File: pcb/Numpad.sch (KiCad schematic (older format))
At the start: 61 parts, among them P1 USB-MICRO-B, P2 HOLE, P3 HOLE, P4 HOLE, P5 HOLE, SW1 F13, SW10 8, SW11 9, SW12 PLUS, SW13 4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

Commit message: Macrofab order
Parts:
- C2, C3: value 18p -> 8p
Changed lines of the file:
@@
 P 5650 5150
 F 0 "C2" H 5675 5250 50  0000 L CNN
-F 1 "18p" H 5675 5050 50  0000 L CNN
+F 1 "8p" H 5675 5050 50  0000 L CNN
 F 2 "Keyboard:C_0805" H 5688 5000 50  0001 C CNN
 F 3 "" H 5650 5150 50  0000 C CNN
@@
 P 6550 5150
 F 0 "C3" H 6575 5250 50  0000 L CNN
-F 1 "18p" H 6575 5050 50  0000 L CNN
+F 1 "8p" H 6575 5050 50  0000 L CNN
 F 2 "Keyboard:C_0805" H 6588 5000 50  0001 C CNN
 F 3 "" H 6550 5150 50  0000 C CNN
@@
 $EndComp
 $Comp
-L +5V #PWR09
+L +5V #PWR08
 U 1 1 57D75692
 P 10000 5000
-F 0 "#PWR09" H 10000 4850 50  0001 C CNN
+F 0 "#PWR08" H 10000 4850 50  0001 C CNN
 F 1 "+5V" H 10000 5140 50  0000 C CNN
 F 2 "" H 10000 5000 50  0000 C CNN
@@
 $EndComp
 $Comp
-L GND #PWR010
+L GND #PWR09
 U 1 1 57D75718
 P 10000 5600
-F 0 "#PWR010" H 10000 5350 50  0001 C CNN
+F 0 "#PWR09" H 10000 5350 50  0001 C CNN
 F 1 "GND" H 10000 5450 50  0000 C CNN
 F 2 "" H 10000 5600 50  0000 C CNN
@@
 $EndComp
 $Comp
-L GND #PWR012
+L GND #PWR010
 U 1 1 583FE5A3
 P 8150 4850
-F 0 "#PWR012" H 8150 4600 50  0001 C CNN
+F 0 "#PWR010" H 8150 4600 50  0001 C CNN
 F 1 "GND" H 8150 4700 50  0000 C CNN
 F 2 "" H 8150 4850 50  0000 C CNN
@@
 $EndComp
 $Comp
-L GND #PWR013
+L GND #PWR011
 U 1 1 583F8B57
 P 6100 4950
-F 0 "#PWR013" H 6100 4700 50  0001 C CNN
+F 0 "#PWR011" H 6100 4700 50  0001 C CNN
 F 1 "GND" H 6100 4800 50  0000 C CNN
 F 2 "" H 6100 4950 50  0000 C CNN
@@
 $EndComp
 $Comp
-L GND #PWR014
+L GND #PWR012
 U 1 1 5840D946
 P 9450 3900
-F 0 "#PWR014" H 9450 3650 50  0001 C CNN
+F 0 "#PWR012" H 9450 3650 50  0001 C CNN
 F 1 "GND" H 9450 3750 50  0000 C CNN
 F 2 "" H 9450 3900 50  0000 C CNN
@@
 $EndComp
 $Comp
-L +5V #PWR015
+L +5V #PWR013
 U 1 1 587461EE
 P 5700 1000
-F 0 "#PWR015" H 5700 850 50  0001 C CNN
+F 0 "#PWR013" H 5700 850 50  0001 C CNN
 F 1 "+5V" H 5700 1140 50  0000 C CNN
 F 2 "" H 5700 1000 50  0000 C CNN
@@
 $EndComp
 $Comp
-L +5V #PWR016
+L +5V #PWR014
 U 1 1 5874632C
 P 6050 2700
-F 0 "#PWR016" H 6050 2550 50  0001 C CNN
+F 0 "#PWR014" H 6050 2550 50  0001 C CNN
 F 1 "+5V" H 6050 2840 50  0000 C CNN
 F 2 "" H 6050 2700 50  0000 C CNN

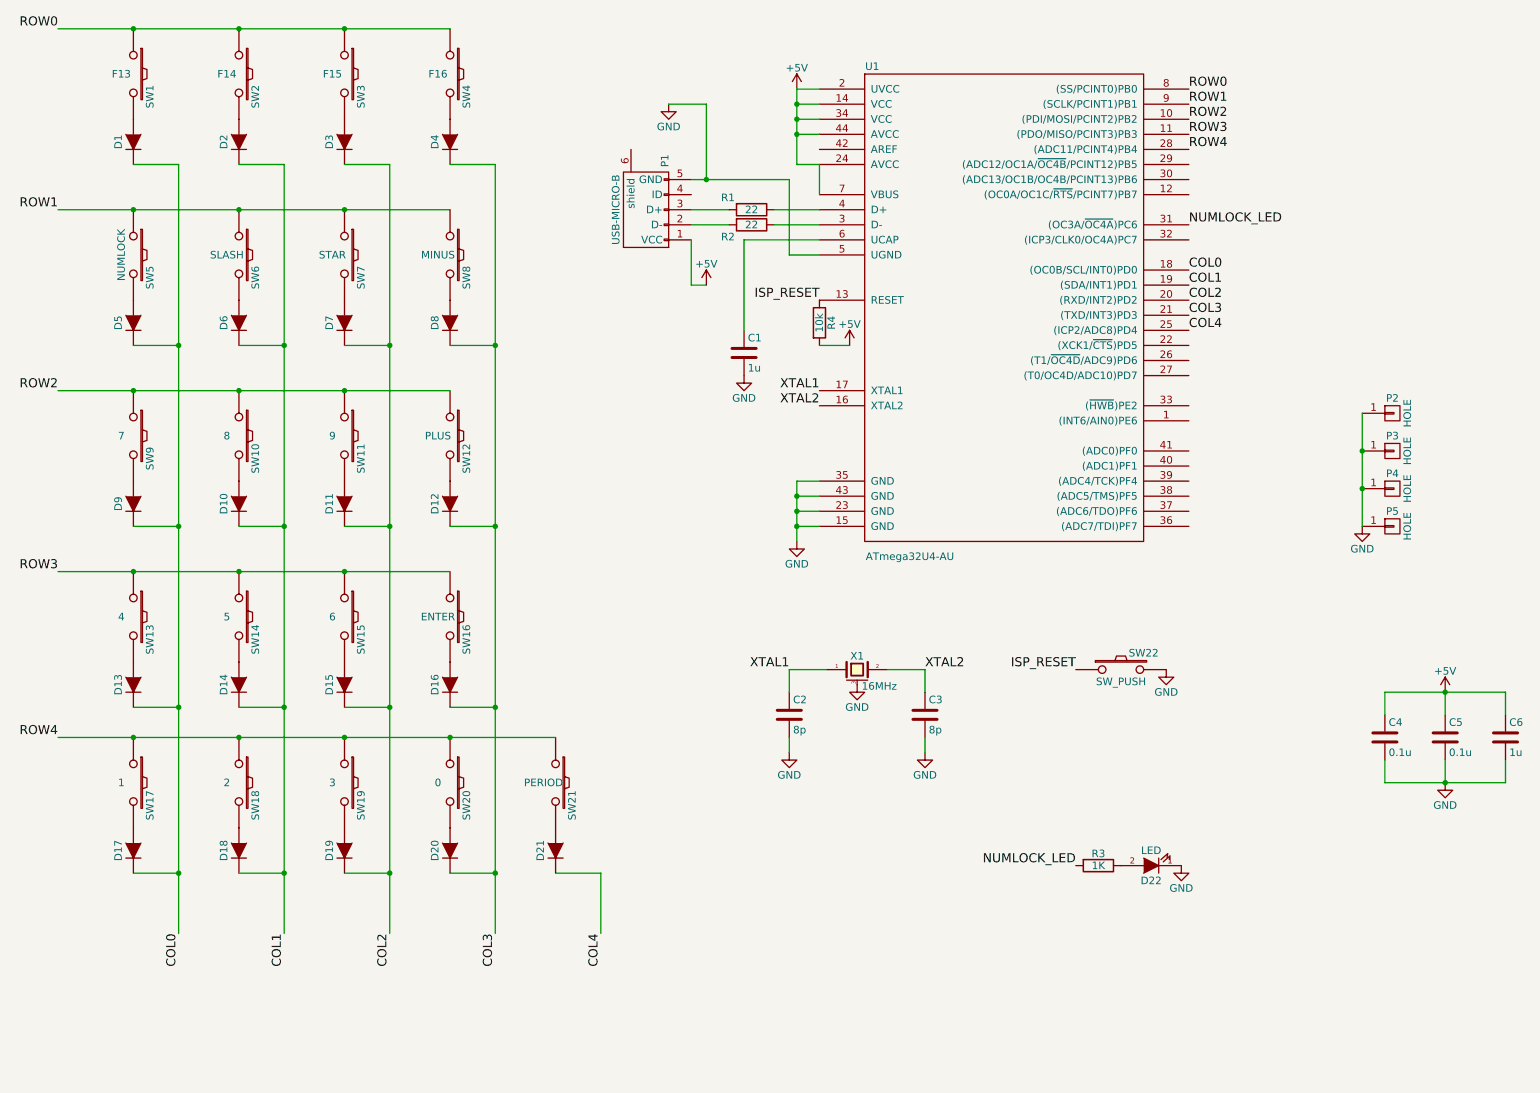
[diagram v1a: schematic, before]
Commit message: Remove atmega32u4 and related components
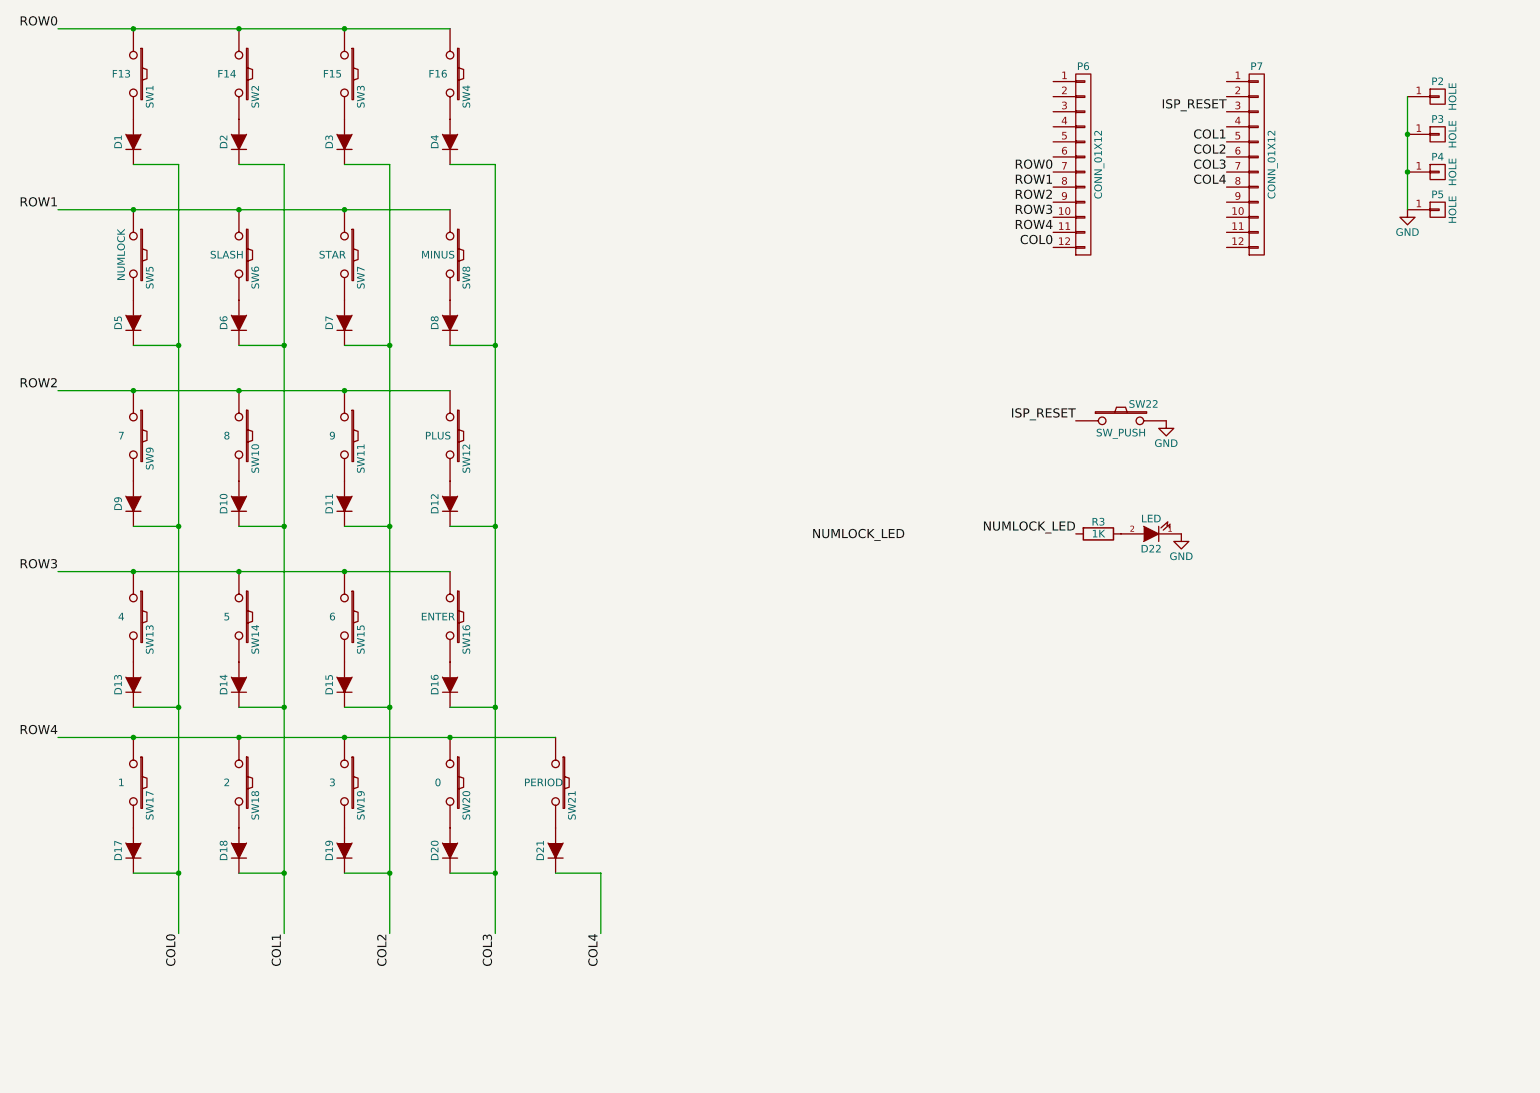
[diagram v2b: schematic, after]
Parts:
- removed C1, C6: 1u, Keyboard:C_0805, symbol C
- removed C2, C3: 8p, Keyboard:C_0805, symbol C
- removed C4, C5: 0.1u, Keyboard:C_0805, symbol C
- removed P1: USB-MICRO-B, 10118192-0001LF:10118192-0001LF, symbol USB_OTG
- removed R1, R2: 22, Keyboard:R_0805, symbol R
- removed R4: 10k, Keyboard:R_0805, symbol R
- removed U1: ATmega32U4-AU, ATMEGA32U4-AU:QFP80P1200X1200X120-44N, symbol ATmega32U4-AU
- removed X1: 16MHz, Crystals:Crystal_SMD_5032_4Pads, symbol CRYSTAL_SMD
- added P6, P7: CONN_01X12, Pin_Headers:Pin_Header_Straight_1x12_Pitch2.54mm, symbol CONN_01X12
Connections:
- net COL0: now also P6.12 (P12)
- net COL1: now also P7.5 (P5)
- net COL2: now also P7.6 (P6)
- net COL3: now also P7.7 (P7)
- net COL4: now also P7.8 (P8)
- net ISP_RESET: now also P7.3 (P3)
- net ROW0: now also P6.7 (P7)
- net ROW1: now also P6.8 (P8)
- net ROW2: now also P6.9 (P9)
- net ROW3: now also P6.10 (P10)
- net ROW4: now also P6.11 (P11)
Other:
- moved on the sheet: D22, P2, P3, P4, P5, R3, SW22

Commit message: Complete routes and layout. Need to check Osh Park rules
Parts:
- removed D3, D4: D, Diodes_SMD:SOD-123, symbol D
- removed SW3: F15, Tim's Cherry MX:CHERRY_PLATE_100H, symbol SW_PUSH
- removed SW4: F16, Tim's Cherry MX:CHERRY_PLATE_100H, symbol SW_PUSH
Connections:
- net COL0: now also P6.11 (P11); no longer P6.12 (P12)
- net COL1: now also P6.10 (P10); no longer P7.5 (P5)
- net COL2: now also P6.8 (P8); no longer P7.6 (P6)
- net COL3: now also P7.6 (P6); no longer P7.7 (P7)
- net COL4: now also P7.5 (P5); no longer P7.8 (P8)
- net GND: now also P7.2 (P2)
- net ROW0: now also P6.12 (P12); no longer P6.7 (P7)
- net ROW1: now also P6.9 (P9); no longer P6.8 (P8)
- net ROW2: now also P6.7 (P7); no longer P6.9 (P9)
- net ROW3: now also P7.8 (P8); no longer P6.10 (P10)
- net ROW4: now also P7.7 (P7); no longer P6.11 (P11)
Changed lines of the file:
@@
-$EndComp
-$Comp
-L SW_PUSH SW3
-U 1 1 57D60E45
-P 2700 900
-F 0 "SW3" H 2850 1010 50  0000 C CNN
-F 1 "F15" V 2700 820 50  0000 C CNN
-F 2 "Tim's Cherry MX:CHERRY_PLATE_100H" H 2700 900 50  0001 C CNN
-F 3 "" H 2700 900 50  0000 C CNN
-	1    2700 900
-	0    1    1    0
-$EndComp
-$Comp
-L SW_PUSH SW4
-U 1 1 57D60E4B
-P 3400 900
-F 0 "SW4" H 3550 1010 50  0000 C CNN
-F 1 "F16" V 3400 820 50  0000 C CNN
-F 2 "Tim's Cherry MX:CHERRY_PLATE_100H" H 3400 900 50  0001 C CNN
-F 3 "" H 3400 900 50  0000 C CNN
-	1    3400 900
-	0    1    1    0
 $EndComp
 $Comp
@@
 F 3 "" H 2000 1350 50  0000 C CNN
 	1    2000 1350
-	0    -1   -1   0
-$EndComp
-$Comp
-L D D3
-U 1 1 57D61BB8
-P 2700 1350
-F 0 "D3" H 2700 1450 50  0000 C CNN
-F 1 "D" H 2700 1250 50  0001 C CNN
-F 2 "Diodes_SMD:SOD-123" H 2700 1350 50  0001 C CNN
-F 3 "" H 2700 1350 50  0000 C CNN
-	1    2700 1350
-	0    -1   -1   0
-$EndComp
-$Comp
-L D D4
-U 1 1 57D61C02
-P 3400 1350
-F 0 "D4" H 3400 1450 50  0000 C CNN
-F 1 "D" H 3400 1250 50  0001 C CNN
-F 2 "Diodes_SMD:SOD-123" H 3400 1350 50  0001 C CNN
-F 3 "" H 3400 1350 50  0000 C CNN
-	1    3400 1350
 	0    -1   -1   0
 $EndComp
@@
 $EndComp
 $Comp
-L GND #PWR04
+L GND #PWR02
 U 1 1 583FE5A3
 P 8150 3200
-F 0 "#PWR04" H 8150 2950 50  0001 C CNN
+F 0 "#PWR02" H 8150 2950 50  0001 C CNN
 F 1 "GND" H 8150 3050 50  0000 C CNN
 F 2 "" H 8150 3200 50  0000 C CNN
@@
 $EndComp
 $Comp
-L GND #PWR05
+L GND #PWR03
 U 1 1 5840D946
 P 9750 1800
-F 0 "#PWR05" H 9750 1550 50  0001 C CNN
+F 0 "#PWR03" H 9750 1550 50  0001 C CNN
 F 1 "GND" H 9750 1650 50  0000 C CNN
 F 2 "" H 9750 1800 50  0000 C CNN
@@
 Connection ~ 3700 6200
 Wire Wire Line
-	3400 6200 3700 6200
+	3700 6200 3400 6200
 Connection ~ 3700 5100
 Wire Wire Line
-	3400 5100 3700 5100
+	3700 5100 3400 5100
 Connection ~ 3700 3900
 Wire Wire Line
@@
 	3400 2700 3700 2700
 Wire Wire Line
-	3700 1500 3700 6600
-Wire Wire Line
-	3400 1500 3700 1500
+	3700 2700 3700 6600
 Connection ~ 3000 6200
 Wire Wire Line
-	2700 6200 3000 6200
+	3000 6200 2700 6200
 Connection ~ 3000 5100
 Wire Wire Line
-	2700 5100 3000 5100
+	3000 5100 2700 5100
 Connection ~ 3000 3900
 Wire Wire Line
@@
 Wire Wire Line
 	2700 2700 3000 2700
-Wire Wire Line
-	3000 1500 3000 6600
-Wire Wire Line
-	2700 1500 3000 1500
 Connection ~ 2300 6200
 Wire Wire Line
-	2000 6200 2300 6200
+	2300 6200 2000 6200
 Connection ~ 2300 5100
 Wire Wire Line
-	2000 5100 2300 5100
+	2300 5100 2000 5100
 Connection ~ 2300 3900
 Wire Wire Line
-	2000 3900 2300 3900
+	2300 3900 2000 3900
 Connection ~ 2300 2700
 Wire Wire Line
@@
 Connection ~ 1600 6200
 Wire Wire Line
-	1300 6200 1600 6200
+	1600 6200 1300 6200
 Connection ~ 1600 5100
 Wire Wire Line
@@
 Connection ~ 1600 3900
 Wire Wire Line
-	1300 3900 1600 3900
+	1600 3900 1300 3900
 Wire Wire Line
 	1300 2700 1600 2700
@@
 Wire Wire Line
 	800  1800 3400 1800
-Connection ~ 2700 600
 Connection ~ 2000 600
 Connection ~ 1300 600
 Wire Wire Line
-	800  600  3400 600
+	800  600  2000 600
 $Comp
 L CONN_01X12 P6
@@
 	1    0    0    -1
 $EndComp
+Text Label 7400 2050 2    60   ~ 0
+ROW0
+Text Label 7400 1750 2    60   ~ 0
+ROW1
 Text Label 7400 1550 2    60   ~ 0
-ROW0
+ROW2
+Text Label 8550 1650 2    60   ~ 0
+ROW3
+Text Label 8550 1550 2    60   ~ 0
+ROW4
+Text Label 7400 1950 2    60   ~ 0
+COL0
+Text Label 7400 1850 2    60   ~ 0
+COL1
 Text Label 7400 1650 2    60   ~ 0
-ROW1
-Text Label 7400 1750 2    60   ~ 0
-ROW2
-Text Label 7400 1850 2    60   ~ 0
-ROW3
-Text Label 7400 1950 2    60   ~ 0
-ROW4
-Text Label 7400 2050 2    60   ~ 0
-COL0
+COL2
+Text Label 8550 1450 2    60   ~ 0
+COL3
 Text Label 8550 1350 2    60   ~ 0
-COL1
-Text Label 8550 1450 2    60   ~ 0
-COL2
-Text Label 8550 1550 2    60   ~ 0
-COL3
-Text Label 8550 1650 2    60   ~ 0
 COL4
 Text Label 8550 1150 2    60   ~ 0
 ISP_RESET
+$Comp
+L GND #PWR04
+U 1 1 58F98263
+P 8050 1050
+F 0 "#PWR04" H 8050 800 50  0001 C CNN
+F 1 "GND" H 8050 900 50  0000 C CNN
+F 2 "" H 8050 1050 50  0000 C CNN
+F 3 "" H 8050 1050 50  0000 C CNN
+	1    8050 1050
+	1    0    0    -1
+$EndComp
+Wire Wire Line
+	8550 1050 8050 1050
+Wire Wire Line
+	3000 2700 3000 6600
 $EndSCHEMATC

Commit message: Wire up Numlock LED
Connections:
- net NUMLOCK_LED: now also P7.12 (P12)
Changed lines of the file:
@@
 	1    0    0    -1
 $EndComp
-Text Label 5800 4000 0    60   ~ 0
+Text Label 8550 2050 2    60   ~ 0
 NUMLOCK_LED
 Text Label 7550 3950 2    60   ~ 0

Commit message: Change wires to match prototype, add pullups for columns
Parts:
- added R4, R5, R6, R7, R8, R9: R, Keyboard:R_0805, symbol R
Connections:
- net COL0: now also P6.6 (P6); no longer P6.11 (P11)
- net COL1: now also P6.5 (P5); no longer P6.10 (P10)
- net COL2: now also P6.2 (P2); no longer P6.8 (P8)
- net COL3: now also P6.1 (P1); no longer P7.6 (P6)
- net COL4: now also P6.7 (P7); no longer P7.5 (P5)
- net ISP_RESET: now also R4.1
- net NUMLOCK_LED: now also P7.8 (P8); no longer P7.12 (P12)
- net ROW0: now also P7.9 (P9), R5.2; no longer P6.12 (P12)
- net ROW1: now also P7.11 (P11), R6.2; no longer P6.9 (P9)
- net ROW2: now also P7.10 (P10), R7.2; no longer P6.7 (P7)
- net ROW3: now also P6.11 (P11), R8.2; no longer P7.8 (P8)
- net ROW4: now also P6.12 (P12), R9.2; no longer P7.7 (P7)
- net VCC: now reaches P7.4 (P4)
- net VCC: now also R4.2, R5.1, R6.1, R7.1, R8.1, R9.1
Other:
- moved on the sheet: D1, D10, D11, D12, D13, D14, D15, D16, D17, D18, D19, D2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
